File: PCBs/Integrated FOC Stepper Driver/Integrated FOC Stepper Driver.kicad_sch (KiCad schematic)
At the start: 34 parts, among them J1 JST PH 01x04, J2 USB C Receptacle, SW1 BOOT, SW2 RESET, U1 RP2040, U2 MT6701CT, U5 W25Q128JVS, Y1 12MHz/12pF/50Ω/20ppm

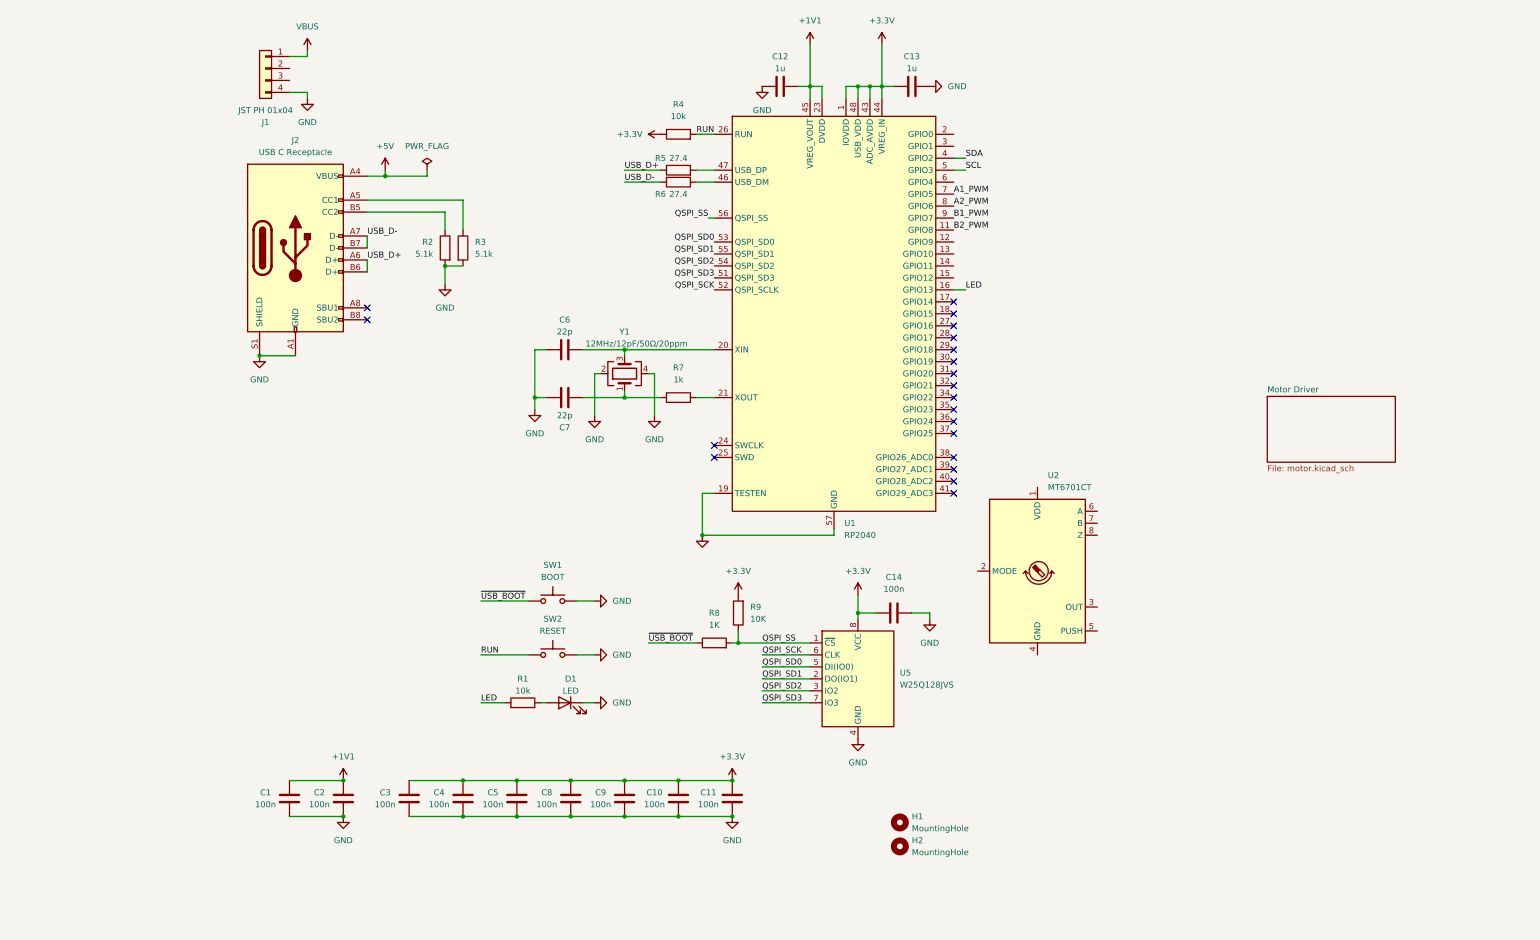
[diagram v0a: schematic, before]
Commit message: Rearrange schematic, start adding CAN bus hardware
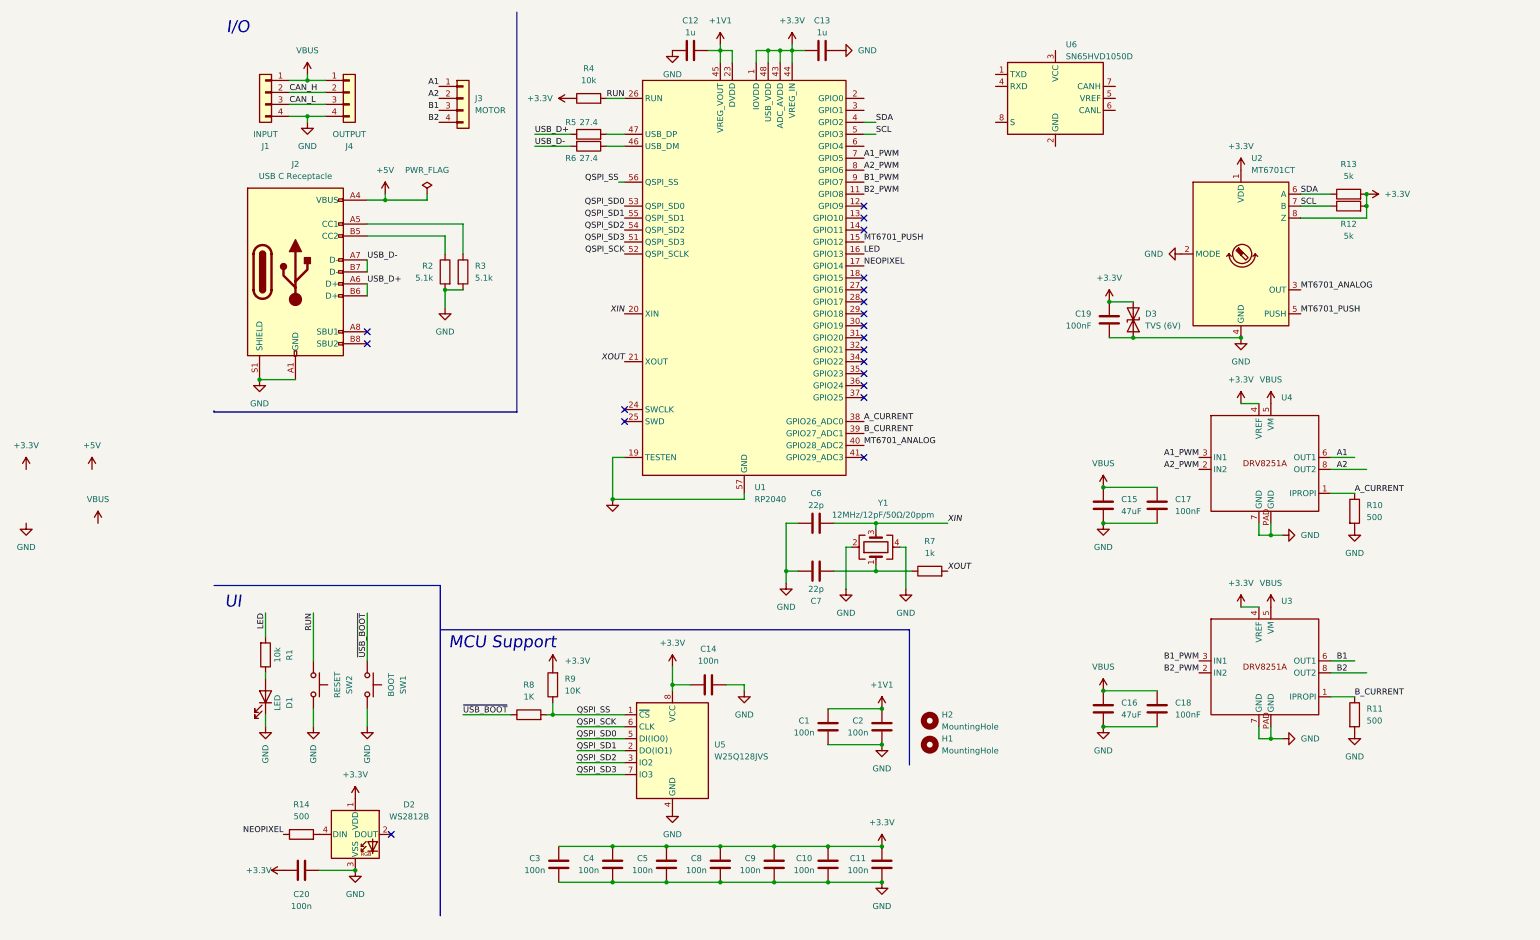
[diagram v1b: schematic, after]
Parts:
- added C15, C16: 47uF, symbol Device:C
- added C17, C18, C19: 100nF, symbol Device:C
- added C20: 100n, symbol Device:C
- added D2: WS2812B, LED_SMD:LED_WS2812B_PLCC4_5.0x5.0mm_P3.2mm, symbol LED:WS2812B
- added D3: TVS (6V), symbol Device:D_TVS
- added J3: MOTOR, Connector_JST:JST_XH_S4B-XH-SM4-TB_1x04-1MP_P2.50mm_Horizontal, symbol Connector_Generic:Conn_01x04
- added J4: OUTPUT, Connector_JST:JST_XH_S4B-XH-SM4-TB_1x04-1MP_P2.50mm_Horizontal, symbol Connector_Generic:Conn_01x04
- added R10, R11, R14: 500, Resistor_SMD:R_0805_2012Metric_Pad1.20x1.40mm_HandSolder, symbol Device:R
- added R12, R13: 5k, symbol Device:R
- added U3, U4: ~, Package_SO:Texas_HSOP-8-1EP_3.9x4.9mm_P1.27mm_ThermalVias, symbol EchoSymbols:DRV8251A
- added U6: SN65HVD1050D, Package_SO:SOIC-8_3.9x4.9mm_P1.27mm, symbol Interface_CAN_LIN:SN65HVD1050D
- C1, C10, C11, C12, C13, C14, C2, C3, C4, C5, C6, C7, C8, C9: footprint Capacitor_SMD:C_0402_1005Metric -> Capacitor_SMD:C_0603_1608Metric_Pad1.08x0.95mm_HandSolder
- D1: footprint LED_SMD:LED_0402_1005Metric -> LED_SMD:LED_0603_1608Metric_Pad1.05x0.95mm_HandSolder
- J1: value JST PH 01x04 -> INPUT; footprint Connector_JST:JST_PH_S4B-PH-K_1x04_P2.00mm_Horizontal -> Connector_JST:JST_XH_S4B-XH-SM4-TB_1x04-1MP_P2.50mm_Horizontal
- R1, R2, R3, R4, R5, R6, R7, R8, R9: footprint Resistor_SMD:R_0402_1005Metric -> Resistor_SMD:R_0603_1608Metric_Pad0.98x0.95mm_HandSolder
- U2: LCSC (none) -> C19711153
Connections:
- net +3.3V: now also U2.1 (VDD), U2.8 (Z), C19.1, C20.1, D2.1 (VDD), D3.2 (A2), R12.2, R13.2, U3.4 (VREF), U4.4 (VREF)
- net A1_PWM: now also U4.3 (IN1)
- net A2_PWM: now also U4.2 (IN2)
- net B1_PWM: now also U3.3 (IN1)
- net B2_PWM: now also U3.2 (IN2)
- net GND: now also U2.2 (MODE), U2.4 (GND), C15.2, C16.2, C17.2, C18.2, C19.2, C20.2, D2.3 (VSS), D3.1 (A1), J4.4 (Pin_4), R10.2, R11.2, U3.7 (GND), U3.PAD (GND), U4.7 (GND), U4.PAD (GND)
- net SCL: now also U2.7 (B), R12.1
- net SDA: now also U2.6 (A), R13.1
- net VBUS: now also C15.1, C16.1, C17.1, C18.1, J4.1 (Pin_1), U3.5 (VM), U4.5 (VM)
- net XIN: now reaches C6.2, U1.20 (XIN), Y1.3
- net XOUT: now reaches R7.2, U1.21 (XOUT)
- net CAN_H: now reaches J1.2 (Pin_2)
- net CAN_H: now also J4.2 (Pin_2)
- net CAN_L: now reaches J1.3 (Pin_3)
- net CAN_L: now also J4.3 (Pin_3)
- net MT6701_ANALOG: now reaches U2.3 (OUT)
- net MT6701_ANALOG: now also U1.40 (GPIO28_ADC2)
- net MT6701_PUSH: now reaches U2.5 (PUSH)
- net MT6701_PUSH: now also U1.15 (GPIO12)
- net NEOPIXEL: now reaches U1.17 (GPIO14)
- net NEOPIXEL: now also R14.1
- net A_CURRENT: now reaches U1.38 (GPIO26_ADC0)
- net A_CURRENT: now also R10.1, U4.1 (IPROPI)
- net B_CURRENT: now reaches U1.39 (GPIO27_ADC1)
- net B_CURRENT: now also R11.1, U3.1 (IPROPI)
- new net: D2.4 (DIN), R14.2
- new net A1: J3.1 (Pin_1), U4.6 (OUT1)
- new net A2: J3.2 (Pin_2), U4.8 (OUT2)
- new net B1: J3.3 (Pin_3), U3.6 (OUT1)
- new net B2: J3.4 (Pin_4), U3.8 (OUT2)
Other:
- removed sheet Motor Driver
- note added: "I/O"
- note added: "MCU Support"
- note added: "UI"
- company: (none) -> UC Berkeley MECENG 135/235
- title: (none) -> Echo FOC Stepper Driver
- moved on the sheet: C1, C10, C11, C12, C13, C14, C2, C3, C4, C5, C6, C7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

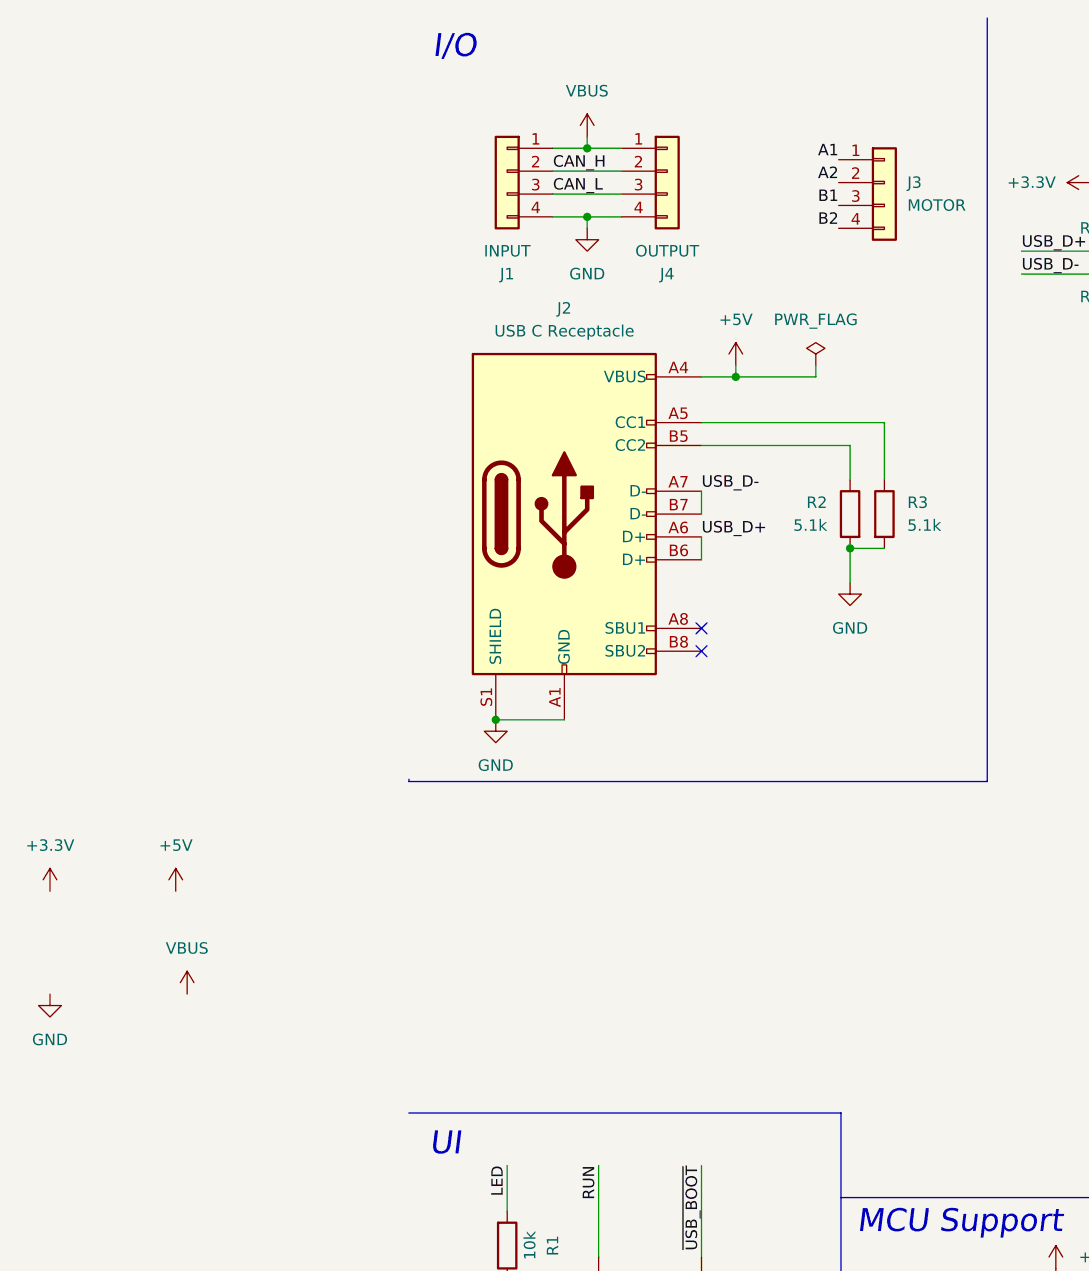
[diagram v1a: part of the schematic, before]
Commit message: Set up LDOs
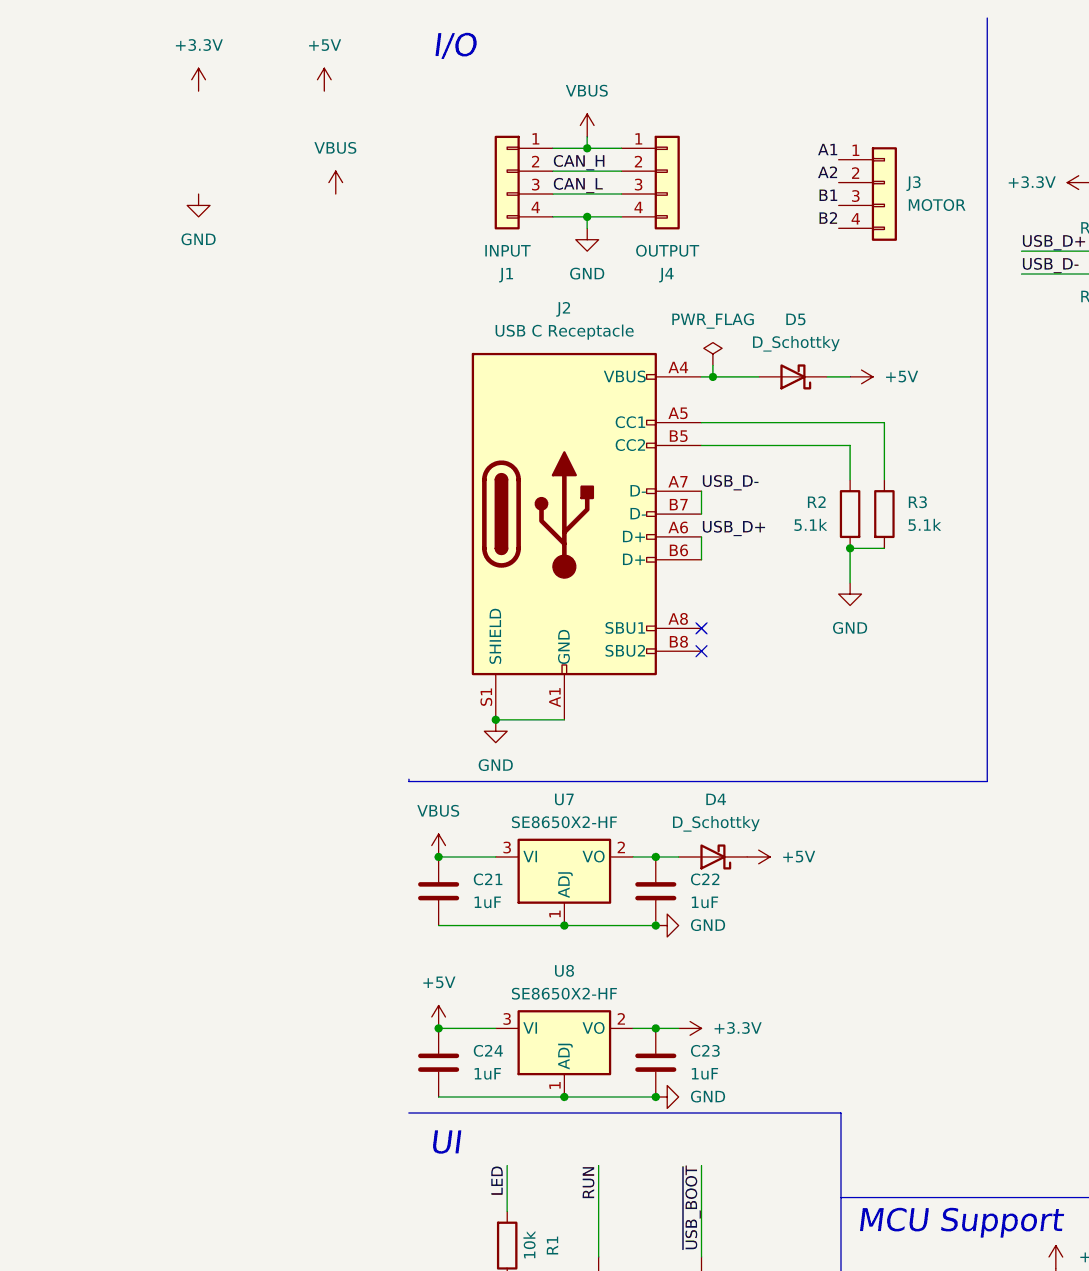
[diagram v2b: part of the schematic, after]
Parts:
- added C21, C22, C23, C24: 1uF, symbol Device:C
- added D4, D5: D_Schottky, symbol Device:D_Schottky
- added U7, U8: SE8650X2-HF, Package_TO_SOT_SMD:SOT-23_Handsoldering, symbol Regulator_Linear:AMS1117
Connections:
- net +3.3V: now also C23.1, U8.2 (VO)
- net +5V: now also C24.1, D4.1 (K), D5.1 (K), U8.3 (VI); no longer J2.A4 (VBUS), J2.A9 (VBUS), J2.B4 (VBUS), J2.B9 (VBUS)
- net GND: now also C21.2, C22.2, C23.2, C24.2, U7.1 (ADJ), U8.1 (ADJ)
- net VBUS: now also C21.1, U7.3 (VI)
- new net: D5.2 (A), J2.A4 (VBUS), J2.A9 (VBUS), J2.B4 (VBUS), J2.B9 (VBUS)
- new net: C22.1, D4.2 (A), U7.2 (VO)

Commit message: Start layout
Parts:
- added H1, H2: MountingHole, MountingHole:MountingHole_3.2mm_M3_DIN965_Pad, symbol Mechanical:MountingHole
- added J5: Conn_01x02, Connector_PinHeader_2.54mm:PinHeader_1x02_P2.54mm_Vertical, symbol Connector_Generic:Conn_01x02
- added R11: 120, Resistor_SMD:R_0603_1608Metric_Pad0.98x0.95mm_HandSolder, symbol Device:R
- C1: renamed from C21; footprint (none) -> Capacitor_SMD:C_0603_1608Metric_Pad1.08x0.95mm_HandSolder
- C2: renamed from C24; footprint (none) -> Capacitor_SMD:C_0603_1608Metric_Pad1.08x0.95mm_HandSolder
- C20: renamed from C15; footprint (none) -> Capacitor_SMD:C_0603_1608Metric_Pad1.08x0.95mm_HandSolder
- C21: renamed from C16; footprint (none) -> Capacitor_SMD:C_0603_1608Metric_Pad1.08x0.95mm_HandSolder
- C22: renamed from C19; footprint (none) -> Capacitor_SMD:C_0603_1608Metric_Pad1.08x0.95mm_HandSolder
- C23: renamed from C17; footprint (none) -> Capacitor_SMD:C_0603_1608Metric_Pad1.08x0.95mm_HandSolder
- C24: renamed from C18; footprint (none) -> Capacitor_SMD:C_0603_1608Metric_Pad1.08x0.95mm_HandSolder
- C3: renamed from C20; footprint (none) -> Capacitor_SMD:C_0603_1608Metric_Pad1.08x0.95mm_HandSolder
- C4: renamed from C22; footprint (none) -> Capacitor_SMD:C_0603_1608Metric_Pad1.08x0.95mm_HandSolder
- C5: renamed from C23; footprint (none) -> Capacitor_SMD:C_0603_1608Metric_Pad1.08x0.95mm_HandSolder
- D3: renamed from D4; footprint (none) -> Diode_SMD:D_SMA_Handsoldering; LCSC (none) -> C8678
- D4: renamed from D5; footprint (none) -> Diode_SMD:D_SMA_Handsoldering; LCSC (none) -> C8678
- J1: footprint Connector_JST:JST_XH_S4B-XH-SM4-TB_1x04-1MP_P2.50mm_Horizontal -> Connector_JST:JST_PH_S4B-PH-SM4-TB_1x04-1MP_P2.00mm_Horizontal
- J3: renamed from J4; footprint Connector_JST:JST_XH_S4B-XH-SM4-TB_1x04-1MP_P2.50mm_Horizontal -> Connector_JST:JST_PH_S4B-PH-SM4-TB_1x04-1MP_P2.00mm_Horizontal
- J4: renamed from J3; footprint Connector_JST:JST_XH_S4B-XH-SM4-TB_1x04-1MP_P2.50mm_Horizontal -> Connector_JST:JST_PH_S4B-PH-SM4-TB_1x04-1MP_P2.00mm_Horizontal
- R12: renamed from R13; footprint (none) -> Resistor_SMD:R_0603_1608Metric_Pad0.98x0.95mm_HandSolder
- R13: renamed from R12; footprint (none) -> Resistor_SMD:R_0603_1608Metric_Pad0.98x0.95mm_HandSolder
- renumbered C14 to C10, C8 to C11, C9 to C12, C6 to C13, C7 to C14, C13 to C15, C1 to C16, C10 to C17, C2 to C18, C11 to C19, C3 to C6, C4 to C7, C5 to C8, C12 to C9, D3 to D5, H2 to H3, H1 to H4, R7 to R10, R10 to R14, R11 to R15, R14 to R2, R2 to R3, R3 to R4, R8 to R5, R9 to R6, R4 to R7, R5 to R8, R6 to R9, SW2 to SW1, SW1 to SW2, U7 to U1, U8 to U2, U5 to U3, U1 to U4, U6 to U5, U2 to U6, U4 to U7, U3 to U8
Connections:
- net +5V: now also U5.3 (VCC)
- net A1_PWM: now also U4.8 (GPIO6); no longer U4.7 (GPIO5)
- net A2_PWM: now also U4.9 (GPIO7); no longer U4.8 (GPIO6)
- net B1_PWM: now also U4.11 (GPIO8); no longer U4.9 (GPIO7)
- net B2_PWM: now also U4.12 (GPIO9); no longer U4.11 (GPIO8)
- net CAN_H: now also U5.7 (CANH), J5.1 (Pin_1)
- net CAN_L: now also U5.6 (CANL), R11.1
- net GND: now also U5.2 (GND)
- net CAN_TX: now reaches U4.2 (GPIO0)
- net CAN_TX: now also U5.1 (TXD)
- net CAN_S: now reaches U4.27 (GPIO16)
- net CAN_S: now also U5.8 (S)
- net CAN_RX: now reaches U4.3 (GPIO1)
- net CAN_RX: now also U5.4 (RXD)
- new net: J5.2 (Pin_2), R11.2
- no-connect marks 20 -> 21
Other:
- moved on the sheet: U5
